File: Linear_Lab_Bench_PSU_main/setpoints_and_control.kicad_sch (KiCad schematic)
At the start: 53 parts, among them J3 Conn_01x03_Male, J4 Conn_01x03_Male, J5 Conn_01x03_Male, J6 Conn_01x03_Male, J7 Conn_01x02_Male, J8 Conn_01x02_Male, J9 Conn_01x02_Male, Q14 2N4401, Q15 2N4401, U10 LM317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

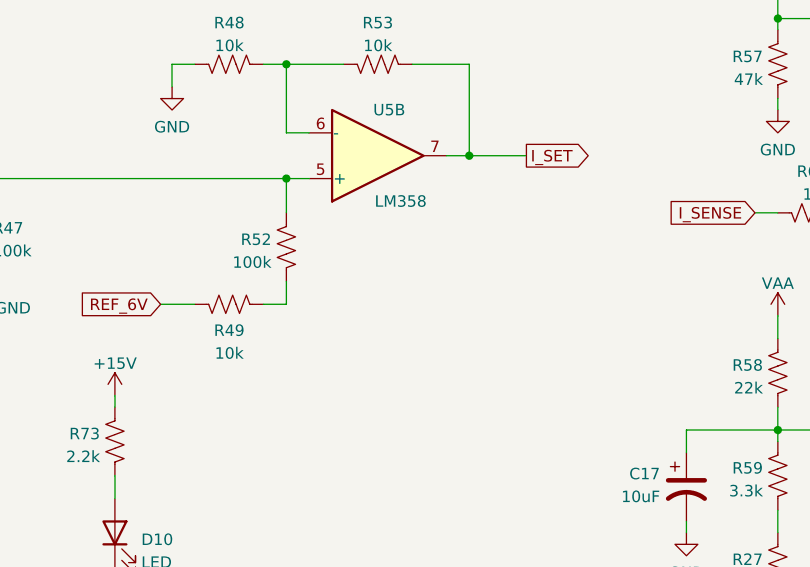
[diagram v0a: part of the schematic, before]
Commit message: Notes on schematic for resistor changes
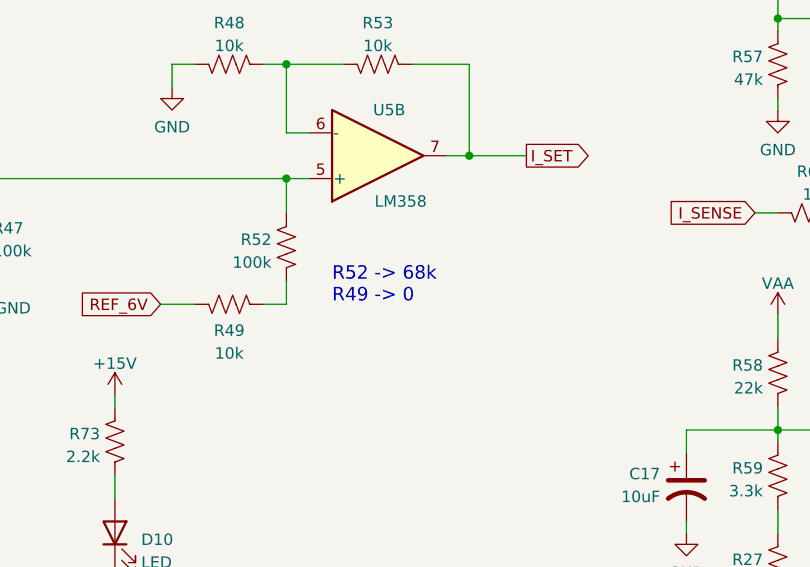
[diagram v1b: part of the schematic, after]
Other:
- note added: "R52 -> 68k R49 -> 0"
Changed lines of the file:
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@@
+    (effects (font (size 1.5 1.5)) (justify left bottom))
+  )
+  (text "R52 -> 68k\nR49 -> 0\n" (at 100.33 114.3 0)
     (effects (font (size 1.5 1.5)) (justify left bottom))
   )
